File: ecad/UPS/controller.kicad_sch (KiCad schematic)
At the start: 36 parts, among them J4 PROG, U4 STM32L152RCT6, U5 AP2112K-3.3TRG1, U6 BOOT0, U7 NRST

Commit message: Final schematic, added fan, shrunk board down about 25%
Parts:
- added D11: 1N4148, Diode_THT:D_DO-35_SOD27_P7.62mm_Horizontal, symbol Diode:1N4148
- added J7: Fan_Connector, LED_THT:LED_D5.0mm_IRGrey, symbol Connector:Conn_01x02_Pin
- added Q8: 2N7002, Package_TO_SOT_SMD:SOT-23, symbol Transistor_FET:2N7002
- added R43: 100, Resistor_SMD:R_0603_1608Metric, symbol Device:R
- added R44: 10K, Resistor_SMD:R_0201_0603Metric_Pad0.64x0.40mm_HandSolder, symbol Device:R
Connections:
- net +5V: now also D11.1 (K), J7.1 (Pin_1)
- net GND: now also Q8.2 (S), R44.1
- net PB0: now reaches U4.26 (PB0)
- net PB0: now also R43.1
- new net: D11.2 (A), J7.2 (Pin_2), Q8.3 (D)
- new net: Q8.1 (G), R43.2, R44.2

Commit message: Rename all grounds to GND
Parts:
- renumbered C61 to C1, C65 to C10, C4 to C2, COUT1 to C3, CIN1 to C4, C63 to C5, C62 to C6, C50 to C7, C49 to C8, C27 to C9, D6 to D1, D10 to D1, D9 to D2, D8 to D4, J4 to J2, R23 to R1, R9 to R10, R33 to R11, R22 to R12, R21 to R13, R20 to R14, R36 to R15, R37 to R16, R42 to R17, R29 to R2, R19 to R3, R18 to R4, R39 to R5, R16 to R6, R15 to R7, R12 to R8, R10 to R9, U4 to U1, U5 to U2, U6 to U3, U7 to U4

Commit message: Light PCB work
Also removed NetTie
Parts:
- R44: footprint Resistor_SMD:R_0201_0603Metric_Pad0.64x0.40mm_HandSolder -> Resistor_SMD:R_0603_1608Metric_Pad0.98x0.95mm_HandSolder
- renumbered C9 to C27, C2 to C4, C8 to C49, C7 to C50, C1 to C61, C6 to C62, C5 to C63, C10 to C65, C4 to CIN1, C3 to COUT1, D1 to D10, D1 to D6, D4 to D8, D2 to D9, J2 to J4, R9 to R10, R8 to R12, R7 to R15, R6 to R16, R4 to R18, R3 to R19, R14 to R20, R13 to R21, R12 to R22, R1 to R23, R2 to R29, R11 to R33, R15 to R36, R16 to R37, R5 to R39, R17 to R42, R10 to R9, U1 to U4, U2 to U5, U3 to U6, U4 to U7
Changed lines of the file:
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@@
 		(in_pos_files yes)
 		(dnp no)
-		(property "Reference" "#PWR012"
+		(property "Reference" "#PWR0118"
 			(at 48.26 161.29 0)
 			(hide yes)
@@
 		(in_pos_files yes)
 		(dnp no)
-		(property "Reference" "#PWR013"
+		(property "Reference" "#PWR0119"
 			(at 48.26 147.32 0)
 			(hide yes)
@@
 		(in_pos_files yes)
 		(dnp no)
-		(property "Reference" "#PWR04"
+		(property "Reference" "#PWR0113"
 			(at 228.6 125.73 0)
 			(hide yes)
@@
 		(in_pos_files yes)
 		(dnp no)
-		(property "Reference" "#PWR05"
+		(property "Reference" "#PWR0114"
 			(at 228.6 99.06 0)
 			(hide yes)
@@
 		(in_pos_files yes)
 		(dnp no)
-		(property "Reference" "#PWR024"
+		(property "Reference" "#PWR0124"
 			(at 74.93 34.29 0)
 			(hide yes)
@@
 		(in_pos_files yes)
 		(dnp no)
-		(property "Reference" "R10"
+		(property "Reference" "R9"
 			(at 38.354 117.856 0)
 			(show_name no)
@@
 		(in_pos_files yes)
 		(dnp no)
-		(property "Reference" "D1"
+		(property "Reference" "D6"
 			(at 93.7006 37.2872 90)
 			(show_name no)
@@
 		(dnp no)
 		(fields_autoplaced yes)
-		(property "Reference" "C6"
+		(property "Reference" "C62"
 			(at 138.43 137.1599 0)
 			(hide yes)
@@
 		(in_pos_files yes)
 		(dnp no)
-		(property "Reference" "C1"
+		(property "Reference" "C61"
 			(at 188.1632 121.8184 0)
 			(show_name no)
@@
 		(in_pos_files yes)
 		(dnp no)
-		(property "Reference" "R2"
+		(property "Reference" "R29"
 			(at 227.1014 128.1684 0)
 			(show_name no)
@@
 		(in_pos_files yes)
 		(dnp no)
-		(property "Reference" "R13"
+		(property "Reference" "R21"
 			(at 86.2584 21.8186 0)
 			(hide yes)
@@
 		(in_pos_files yes)
 		(dnp no)
-		(property "Reference" "D2"
+		(property "Reference" "D9"
 			(at 93.7006 23.3172 90)
 			(hide yes)
@@
 		(dnp no)
 		(fields_autoplaced yes)
-		(property "Reference" "C5"
+		(property "Reference" "C63"
 			(at 144.78 137.1599 0)
 			(show_name no)
@@
 		(dnp no)
 		(fields_autoplaced yes)
-		(property "Reference" "C10"
+		(property "Reference" "C65"
 			(at 82.55 48.26 90)
 			(show_name no)
@@
 		(in_pos_files yes)
 		(dnp no)
-		(property "Reference" "R11"
+		(property "Reference" "R33"
 			(at 86.2584 35.7886 0)
 			(show_name no)
@@
 		(in_pos_files yes)
 		(dnp no)
-		(property "Reference" "R12"
+		(property "Reference" "R22"
 			(at 86.2584 29.4386 0)
 			(hide yes)
@@
 		(in_pos_files yes)
 		(dnp no)
-		(property "Reference" "#PWR014"
+		(property "Reference" "#PWR0120"
 			(at 190.5 115.57 0)
 			(hide yes)
@@
 		(in_pos_files yes)
 		(dnp no)
-		(property "Reference" "#PWR09"
+		(property "Reference" "#PWR0121"
 			(at 74.93 16.51 0)
 			(hide yes)
@@
 		(dnp no)
 		(fields_autoplaced yes)
-		(property "Reference" "R4"
+		(property "Reference" "R18"
 			(at 26.67 99.0599 0)
 			(show_name no)
@@
 		(in_pos_files yes)
 		(dnp no)
-		(property "Reference" "#PWR07"
+		(property "Reference" "#PWR0123"
 			(at 74.93 27.94 0)
 			(hide yes)
@@
 		(in_pos_files yes)
 		(dnp no)
-		(property "Reference" "#PWR06"
+		(property "Reference" "#PWR0111"
 			(at 140.97 153.67 0)
 			(hide yes)
@@
 		(dnp no)
 		(fields_autoplaced yes)
-		(property "Reference" "U2"
+		(property "Reference" "U5"
 			(at 73.66 153.67 0)
 			(show_name no)
@@
 		(in_pos_files yes)
 		(dnp no)
-		(property "Reference" "#PWR010"
+		(property "Reference" "#PWR0125"
 			(at 116.84 38.1 0)
 			(hide yes)
@@
 		(in_pos_files yes)
 		(dnp no)
-		(property "Reference" "#PWR?"
+		(property "Reference" "#PWR01"
 			(at 114.3 165.1 0)
 			(hide yes)
@@
 		(in_pos_files yes)
 		(dnp no)
-		(property "Reference" "#PWR02"
+		(property "Reference" "#PWR0116"
 			(at 53.34 172.72 0)
 			(hide yes)
@@
 		(dnp no)
 		(fields_autoplaced yes)
-		(property "Reference" "R16"
+		(property "Reference" "R37"
 			(at 81.28 118.1099 0)
 			(hide yes)
@@
 		(in_pos_files yes)
 		(dnp no)
-		(property "Reference" "D4"
+		(property "Reference" "D8"
 			(at 93.7006 20.7772 90)
 			(hide yes)
@@
 		(in_pos_files yes)
 		(dnp no)
-		(property "Reference" "#PWR015"
+		(property "Reference" "#PWR0126"
 			(at 182.88 64.77 0)
 			(hide yes)
@@
 		(in_pos_files yes)
 		(dnp no)
-		(property "Reference" "D1"
+		(property "Reference" "D10"
 			(at 93.7006 30.9372 90)
 			(hide yes)
@@
 		(dnp no)
 		(fields_autoplaced yes)
-		(property "Reference" "R5"
+		(property "Reference" "R39"
 			(at 85.09 118.1099 0)
 			(show_name no)
@@
 		(dnp no)
 		(fields_autoplaced yes)
-		(property "Reference" "R6"
+		(property "Reference" "R16"
 			(at 71.12 118.1099 0)
 			(hide yes)
@@
 		(dnp no)
 		(fields_autoplaced yes)
-		(property "Reference" "R9"
+		(property "Reference" "R10"
 			(at 52.07 118.1099 0)
 			(hide yes)
@@
 		(dnp no)
 		(fields_autoplaced yes)
-		(property "Reference" "U4"
+		(property "Reference" "U7"
 			(at 254 114.2999 90)
 			(show_name no)
@@
 		(dnp no)
 		(fields_autoplaced yes)
-		(property "Reference" "C8"
+		(property "Reference" "C49"
 			(at 128.27 137.1599 0)
 			(hide yes)
@@
 			)
 		)
-		(property "Footprint" "Resistor_SMD:R_0201_0603Metric_Pad0.64x0.40mm_HandSolder"
+		(property "Footprint" "Resistor_SMD:R_0603_1608Metric_Pad0.98x0.95mm_HandSolder"
 			(at 221.488 57.15 90)
 			(hide yes)
@@
 		(in_pos_files yes)
 		(dnp no)
-		(property "Reference" "#PWR016"
+		(property "Reference" "#PWR0112"
 			(at 182.88 80.01 0)
 			(hide yes)
@@
 		(in_pos_files yes)
 		(dnp no)
-		(property "Reference" "R1"
+		(property "Reference" "R23"
 			(at 189.0014 134.5184 0)
 			(show_name no)
@@
 		(in_pos_files yes)
 		(dnp no)
-		(property "Reference" "#PWR011"
+		(property "Reference" "#PWR0110"
 			(at 190.5 142.24 0)
 			(hide yes)
@@
 		(dnp no)
 		(fields_autoplaced yes)
-		(property "Reference" "C3"
+		(property "Reference" "COUT1"
 			(at 97.79 158.7499 0)
 			(show_name no)
@@
 		(dnp no)
 		(fields_autoplaced yes)
-		(property "Reference" "R3"
+		(property "Reference" "R19"
 			(at 92.71 116.8399 0)
 			(show_name no)
@@
 		(dnp no)
 		(fields_autoplaced yes)
-		(property "Reference" "R8"
+		(property "Reference" "R12"
 			(at 60.96 118.1099 0)
 			(hide yes)
@@
 		(in_pos_files yes)
 		(dnp no)
-		(property "Reference" "J2"
+		(property "Reference" "J4"
 			(at 193.802 66.2432 0)
 			(show_name no)
@@
 		(dnp no)
 		(fields_autoplaced yes)
-		(property "Reference" "U3"
+		(property "Reference" "U6"
 			(at 210.82 121.9199 90)
 			(show_name no)
@@
 		(in_pos_files yes)
 		(dnp no)
-		(property "Reference" "C2"
+		(property "Reference" "C4"
 			(at 226.2632 115.4684 0)
 			(show_name no)
@@
 		(dnp no)
 		(fields_autoplaced yes)
-		(property "Reference" "C4"
+		(property "Reference" "CIN1"
 			(at 52.07 156.2099 0)
 			(show_name no)
@@
 		(in_pos_files yes)
 		(dnp no)
-		(property "Reference" "R14"
+		(property "Reference" "R20"
 			(at 86.2584 19.2786 0)
 			(hide yes)
@@
 		(dnp no)
 		(fields_autoplaced yes)
-		(property "Reference" "C9"
+		(property "Reference" "C27"
 			(at 123.19 137.1599 0)
 			(hide yes)
@@
 		(in_pos_files yes)
 		(dnp no)
-		(property "Reference" "#PWR01"
+		(property "Reference" "#PWR0115"
 			(at 93.98 149.86 0)
 			(hide yes)
@@
 		(dnp no)
 		(fields_autoplaced yes)
-		(property "Reference" "R15"
+		(property "Reference" "R36"
 			(at 76.2 118.1099 0)
 			(hide yes)
@@
 		(dnp no)
 		(fields_autoplaced yes)
-		(property "Reference" "R7"
+		(property "Reference" "R15"
 			(at 66.04 118.1099 0)
 			(hide yes)
@@
 		(dnp no)
 		(fields_autoplaced yes)
-		(property "Reference" "C7"
+		(property "Reference" "C50"
 			(at 133.35 137.1599 0)
 			(hide yes)
@@
 		(in_pos_files yes)
 		(dnp no)
-		(property "Reference" "U1"
+		(property "Reference" "U4"
 			(at 129.54 116.586 0)
 			(show_name no)
@@
 		(dnp no)
 		(fields_autoplaced yes)
-		(property "Reference" "#PWR03"
+		(property "Reference" "#PWR0109"
 			(at 24.13 110.49 0)
 			(hide yes)
@@
 		(in_pos_files yes)
 		(dnp no)
-		(property "Reference" "#PWR08"
+		(property "Reference" "#PWR0122"
 			(at 74.93 20.32 0)
 			(hide yes)
@@
 		(dnp no)
 		(fields_autoplaced yes)
-		(property "Reference" "R17"
+		(property "Reference" "R42"
 			(at 92.7099 53.34 0)
 			(show_name no)
@@
 		)
 	)
-	(embedded_fonts no)
 )

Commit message: late night grind
Add battery and board thermistor circuits on PC0/PC1.

Implement ADC sampling, temperature conversion, and sensor fault reporting.

Enable the STM32 ADC drivers and poll temperatures in the main loop.

Add the OLED connector on PB10/PB11 and update PCB footprints and net assignments.

Add a Raspberry Pi mounting-hole footprint.

Exclude local docs and test folders from Git.
- checked routing
- messed with firmware
- planning final touches
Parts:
- added C71, C72: 100nF, Capacitor_SMD:C_0805_2012Metric, symbol Device:C
- added J10: NTC_10K_B3950, Connector_PinHeader_2.54mm:PinHeader_1x04_P2.54mm_Vertical, symbol Connector_Generic:Conn_01x04
- added J9: OLED_3V3_I2C2, Connector_PinHeader_2.54mm:PinHeader_1x04_P2.54mm_Vertical, symbol Connector_Generic:Conn_01x04
- added R45, R46: 10k 1%, Resistor_SMD:R_0805_2012Metric, symbol Device:R
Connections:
- net +3.3V: now also J9.2 (Pin_2), R45.1, R46.1
- net GND: now also C71.2, C72.2, J10.1 (Pin_1), J10.3 (Pin_3), J9.1 (Pin_1)
- net OLED_SCL: now reaches U4.29 (PB10)
- net OLED_SCL: now also J9.4 (Pin_4)
- net OLED_SDA: now reaches U4.30 (PB11)
- net OLED_SDA: now also J9.3 (Pin_3)
- net TEMP_BAT: now reaches U4.8 (PC0)
- net TEMP_BAT: now also C71.1, J10.2 (Pin_2), R45.2
- net TEMP_BOARD: now reaches U4.9 (PC1)
- net TEMP_BOARD: now also C72.1, J10.4 (Pin_4), R46.2
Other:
- note added: "Adafruit 4440 + 4397 cable; 100 kHz J9: 1 GND / 2 3V3 / 3 SDA / 4 SCL Module includes pull-ups; no extra resistors"
- note added: "STM32 ADC: PC0 battery / PC1 board External 10k B3950 NTCs: J10 1-2 / 3-4 3.3V only; separate from PD NTC protection"

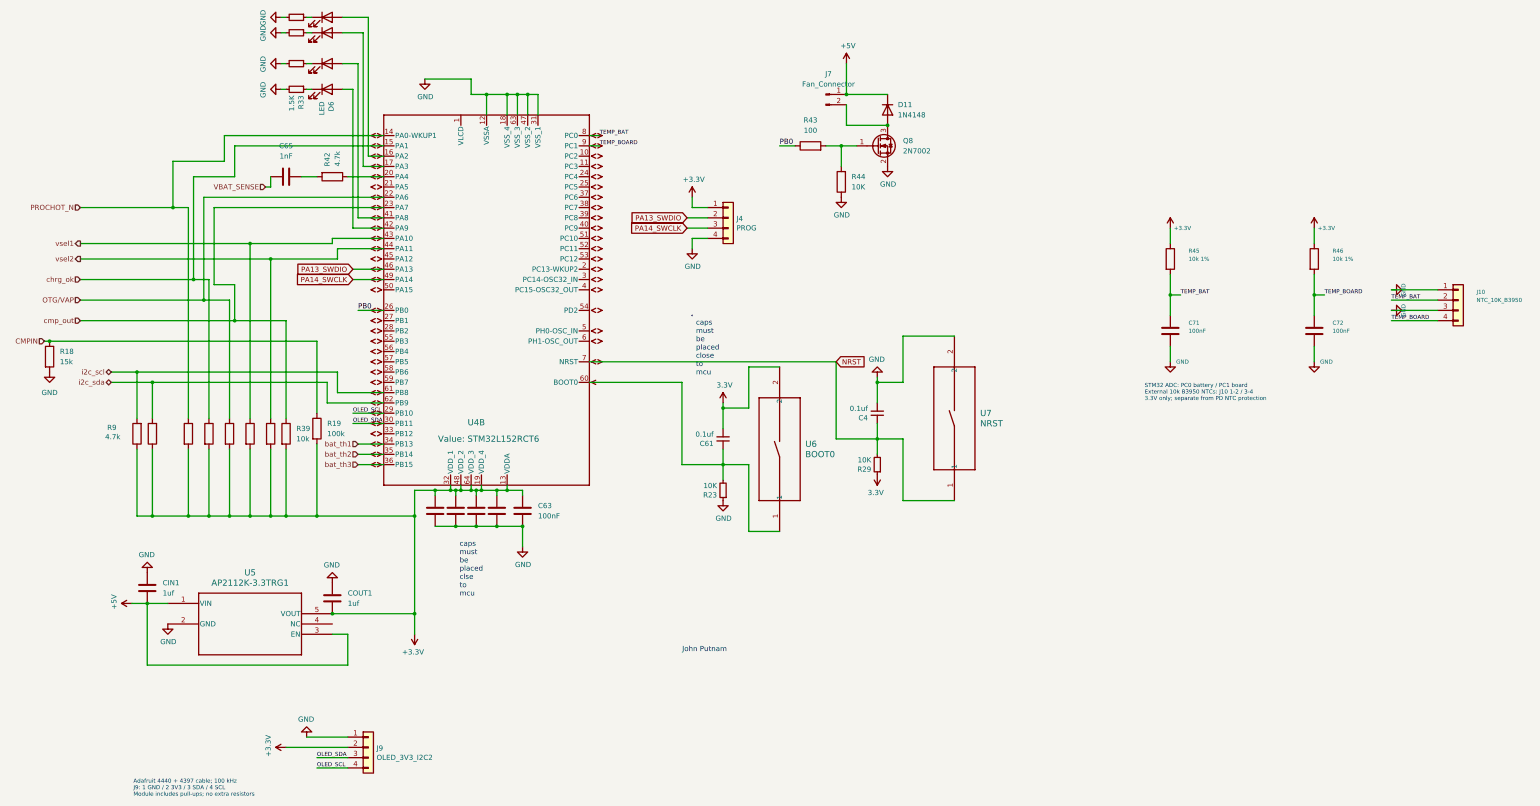
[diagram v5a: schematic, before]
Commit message: touches
Add battery and board thermistor circuits on PC0/PC1.

Implement ADC sampling, temperature conversion, and sensor fault reporting.

Enable the STM32 ADC drivers and poll temperatures in the main loop.

Add the OLED connector on PB10/PB11 and update PCB footprints and net assignments.

Add a Raspberry Pi mounting-hole footprint.

Exclude local docs and test folders from Git.

five ADC sensor inputs

fan-control logic.
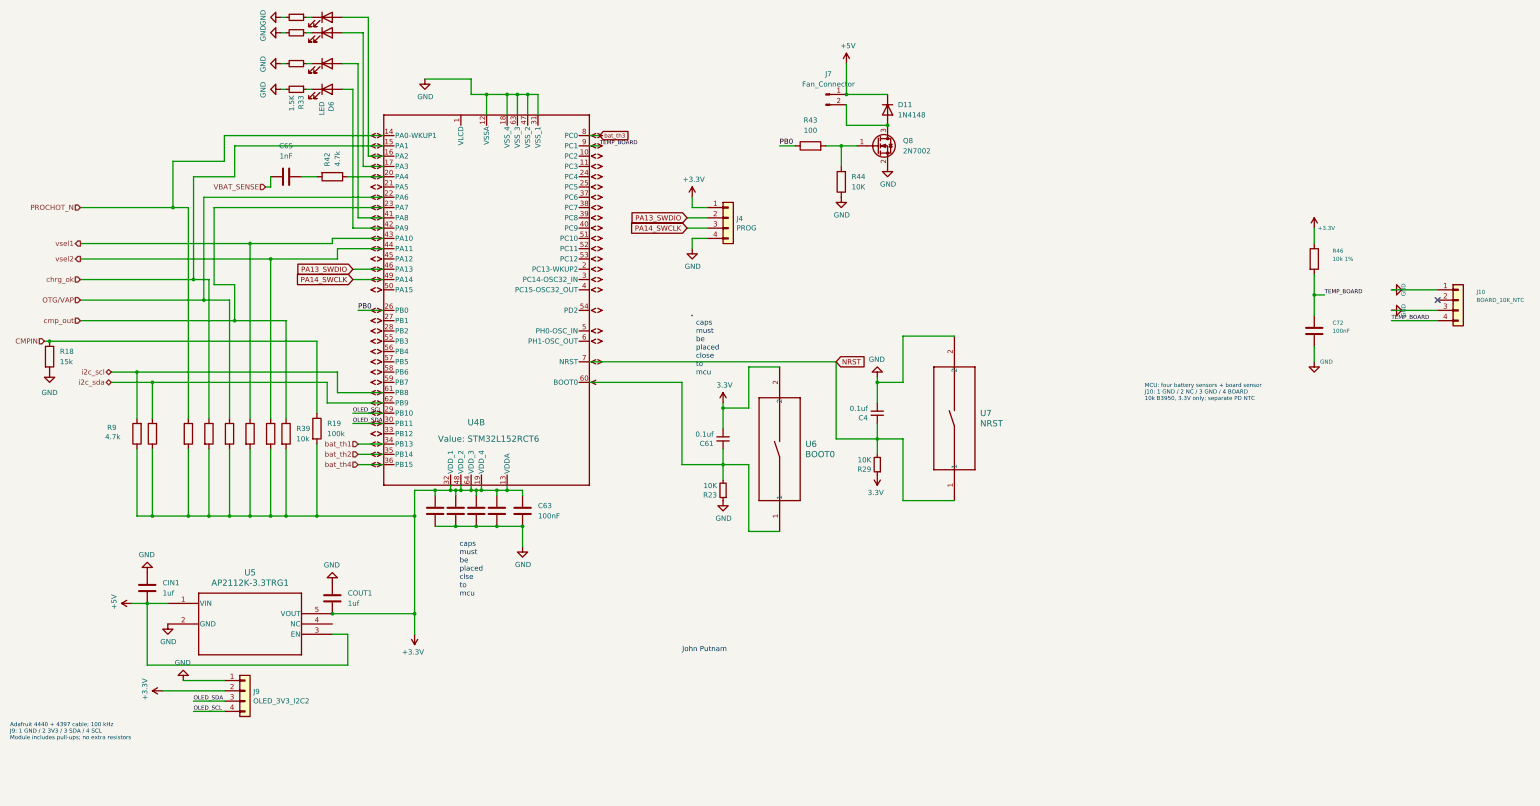
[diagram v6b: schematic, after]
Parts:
- removed C71: 100nF, Capacitor_SMD:C_0805_2012Metric, symbol Device:C
- removed R45: 10k 1%, Resistor_SMD:R_0805_2012Metric, symbol Device:R
- J10: value NTC_10K_B3950 -> BOARD_10K_NTC
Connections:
- net bat_th3: now also U4.8 (PC0); no longer U4.36 (PB15)
- net TEMP_BAT: no longer names the net of J10.2 (Pin_2)
- net TEMP_BAT: no longer U4.8 (PC0)
- new net bat_th4: U4.36 (PB15)
- no-connect marks 0 -> 1
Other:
- note added: "MCU: four battery sensors + board sensor J10: 1 GND / 2 NC / 3 GND / 4 BOARD 10k B3950, 3.3V only; separate PD NTC"
- note removed: "STM32 ADC: PC0 battery / PC1 board External 10k B3950 NTCs: J10 1-2 / 3-4 3.3V only; separate from PD NTC protection"
- moved on the sheet: J9
